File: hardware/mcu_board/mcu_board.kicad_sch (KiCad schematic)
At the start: 1 part, among them J7 MCU

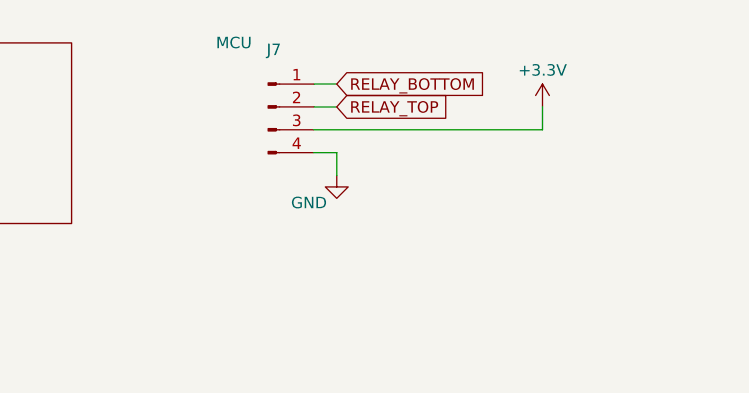
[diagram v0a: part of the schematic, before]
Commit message: Refactored PCBs for v2. See README
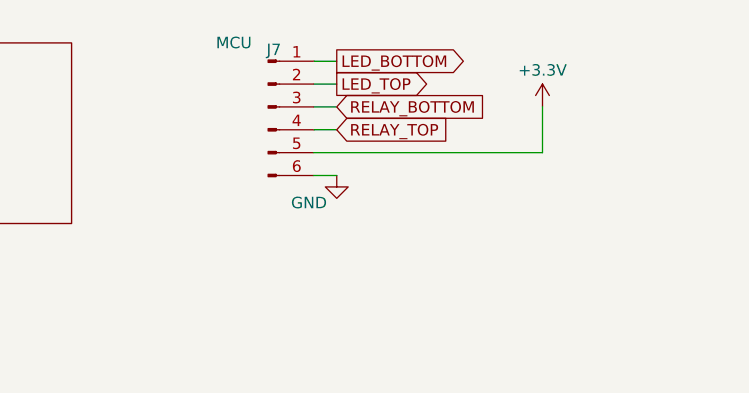
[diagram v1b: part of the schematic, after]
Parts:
- J7: footprint Connector_PinHeader_2.54mm:PinHeader_1x04_P2.54mm_Horizontal -> Connector_PinHeader_2.54mm:PinHeader_1x06_P2.54mm_Horizontal; symbol Connector:Conn_01x04_Pin -> Connector:Conn_01x06_Pin
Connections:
- net +3.3V: now also J7.5 (Pin_5); no longer J7.3 (Pin_3)
- net GND: now also J7.6 (Pin_6); no longer J7.4 (Pin_4)
- net RELAY_BOTTOM: now also J7.3 (Pin_3); no longer J7.1 (Pin_1)
- net RELAY_TOP: now also J7.4 (Pin_4); no longer J7.2 (Pin_2)
- new net LED_BOTTOM: J7.1 (Pin_1)
- new net LED_TOP: J7.2 (Pin_2)
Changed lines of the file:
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@@
 (kicad_sch (version 20230121) (generator eeschema)
   (paper "A4")
-  (wire (pts (xy 144.78 35.56) (xy 147.32 35.56))
-    (stroke (width 0) (type default))
-  )
-  (wire (pts (xy 144.78 43.18) (xy 147.32 43.18))
-    (stroke (width 0) (type default))
-  )
   (wire (pts (xy 144.78 38.1) (xy 147.32 38.1))
     (stroke (width 0) (type default))
   )
-  (wire (pts (xy 144.78 40.64) (xy 170.18 40.64))
+  (wire (pts (xy 144.78 43.18) (xy 170.18 43.18))
     (stroke (width 0) (type default))
   )
-  (wire (pts (xy 170.18 38.1) (xy 170.18 40.64))
+  (wire (pts (xy 144.78 45.72) (xy 147.32 45.72))
     (stroke (width 0) (type default))
   )
-  (wire (pts (xy 147.32 43.18) (xy 147.32 45.72))
+  (wire (pts (xy 144.78 40.64) (xy 147.32 40.64))
+    (stroke (width 0) (type default))
+  )
+  (wire (pts (xy 170.18 38.1) (xy 170.18 43.18))
+    (stroke (width 0) (type default))
+  )
+  (wire (pts (xy 144.78 33.02) (xy 147.32 33.02))
+    (stroke (width 0) (type default))
+  )
+  (wire (pts (xy 144.78 35.56) (xy 147.32 35.56))
     (stroke (width 0) (type default))
   )
@@
     (effects (font (size 1.27 1.27)) (justify left top))
   )
-  (global_label "RELAY_TOP" (shape input) (at 147.32 38.1 0) (fields_autoplaced)
+  (global_label "RELAY_TOP" (shape input) (at 147.32 40.64 0) (fields_autoplaced)
     (effects (font (size 1.27 1.27)) (justify left))
-    (property "Intersheetrefs" "${INTERSHEET_REFS}" (at 160.3858 38.1 0)
+    (property "Intersheetrefs" "${INTERSHEET_REFS}" (at 160.3858 40.64 0)
       (effects (font (size 1.27 1.27)) (justify left) hide)
     )
   )
-  (global_label "RELAY_BOTTOM" (shape input) (at 147.32 35.56 0) (fields_autoplaced)
+  (global_label "LED_TOP" (shape output) (at 147.32 35.56 0) (fields_autoplaced)
     (effects (font (size 1.27 1.27)) (justify left))
-    (property "Intersheetrefs" "${INTERSHEET_REFS}" (at 164.1353 35.56 0)
+    (property "Intersheetrefs" "${INTERSHEET_REFS}" (at 158.288 35.56 0)
+      (effects (font (size 1.27 1.27)) (justify left) hide)
+    )
+  )
+  (global_label "LED_BOTTOM" (shape output) (at 147.32 33.02 0) (fields_autoplaced)
+    (effects (font (size 1.27 1.27)) (justify left))
+    (property "Intersheetrefs" "${INTERSHEET_REFS}" (at 162.0375 33.02 0)
+      (effects (font (size 1.27 1.27)) (justify left) hide)
+    )
+  )
+  (global_label "RELAY_BOTTOM" (shape input) (at 147.32 38.1 0) (fields_autoplaced)
+    (effects (font (size 1.27 1.27)) (justify left))
+    (property "Intersheetrefs" "${INTERSHEET_REFS}" (at 164.1353 38.1 0)
       (effects (font (size 1.27 1.27)) (justify left) hide)
     )
@@
     (pin "1")
     (instances
-      (project "immersion-controller"
+      (project "mcu_board"
         (path "/bd6e6743-d7bb-4018-a688-d589a8d21d49"
           (reference "#PWR01") (unit 1)
@@
     )
   )
-  (symbol (lib_id "Connector:Conn_01x04_Pin") (at 139.7 38.1 0) (unit 1)
+  (symbol (lib_id "Connector:Conn_01x06_Pin") (at 139.7 38.1 0) (unit 1)
     (in_bom yes) (on_board yes) (dnp no)
     (property "Reference" "J7" (at 140.335 31.75 0)
@@
       (effects (font (size 1.27 1.27)))
     )
-    (property "Footprint" "Connector_PinHeader_2.54mm:PinHeader_1x04_P2.54mm_Horizontal" (at 139.7 38.1 0)
+    (property "Footprint" "Connector_PinHeader_2.54mm:PinHeader_1x06_P2.54mm_Horizontal" (at 139.7 38.1 0)
       (effects (font (size 1.27 1.27)) hide)
     )
@@
     (pin "3")
     (pin "4")
+    (pin "5")
+    (pin "6")
     (instances
-      (project "immersion-controller"
+      (project "mcu_board"
         (path "/bd6e6743-d7bb-4018-a688-d589a8d21d49"
           (reference "J7") (unit 1)
@@
     (pin "1")
     (instances
-      (project "immersion-controller"
+      (project "mcu_board"
         (path "/bd6e6743-d7bb-4018-a688-d589a8d21d49"
           (reference "#PWR02") (unit 1)
@@
     )
     (instances
-      (project "immersion-controller"
+      (project "mcu_board"
         (path "/bd6e6743-d7bb-4018-a688-d589a8d21d49" (page "4"))
       )

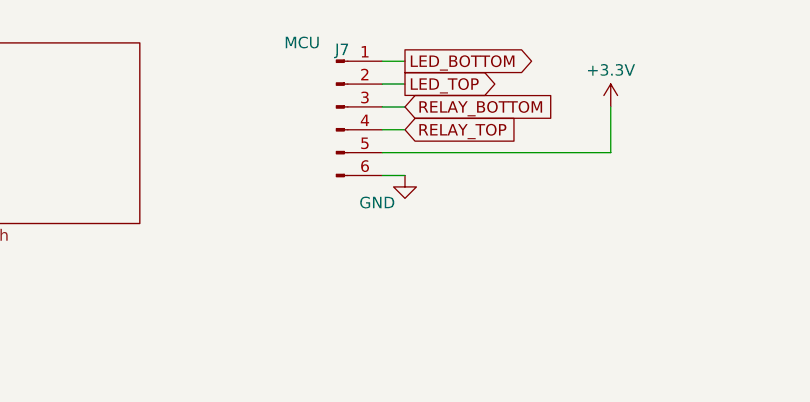
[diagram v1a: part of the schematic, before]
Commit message: v2 layout changes to fit in bax
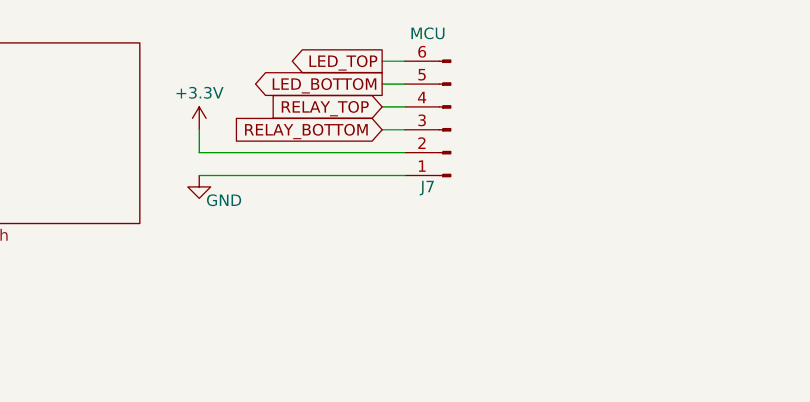
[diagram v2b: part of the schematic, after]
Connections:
- net +3.3V: now also J7.2 (Pin_2); no longer J7.5 (Pin_5)
- net GND: now also J7.1 (Pin_1); no longer J7.6 (Pin_6)
- net LED_BOTTOM: now also J7.5 (Pin_5); no longer J7.1 (Pin_1)
- net LED_TOP: now also J7.6 (Pin_6); no longer J7.2 (Pin_2)
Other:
- moved on the sheet: J7
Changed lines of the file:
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@@
 (kicad_sch (version 20230121) (generator eeschema)
   (paper "A4")
-  (wire (pts (xy 144.78 38.1) (xy 147.32 38.1))
-    (stroke (width 0) (type default))
-  )
-  (wire (pts (xy 144.78 43.18) (xy 170.18 43.18))
-    (stroke (width 0) (type default))
-  )
-  (wire (pts (xy 144.78 45.72) (xy 147.32 45.72))
+  (wire (pts (xy 144.78 33.02) (xy 147.32 33.02))
     (stroke (width 0) (type default))
   )
@@
     (stroke (width 0) (type default))
   )
-  (wire (pts (xy 170.18 38.1) (xy 170.18 43.18))
+  (wire (pts (xy 144.78 35.56) (xy 147.32 35.56))
     (stroke (width 0) (type default))
   )
-  (wire (pts (xy 144.78 33.02) (xy 147.32 33.02))
+  (wire (pts (xy 144.78 38.1) (xy 147.32 38.1))
     (stroke (width 0) (type default))
   )
-  (wire (pts (xy 144.78 35.56) (xy 147.32 35.56))
+  (wire (pts (xy 124.46 45.72) (xy 147.32 45.72))
+    (stroke (width 0) (type default))
+  )
+  (wire (pts (xy 124.46 43.18) (xy 147.32 43.18))
+    (stroke (width 0) (type default))
+  )
+  (wire (pts (xy 124.46 40.64) (xy 124.46 43.18))
     (stroke (width 0) (type default))
   )
@@
     (effects (font (size 1.27 1.27)) (justify left top))
   )
-  (global_label "RELAY_TOP" (shape input) (at 147.32 40.64 0) (fields_autoplaced)
-    (effects (font (size 1.27 1.27)) (justify left))
-    (property "Intersheetrefs" "${INTERSHEET_REFS}" (at 160.3858 40.64 0)
-      (effects (font (size 1.27 1.27)) (justify left) hide)
+  (global_label "RELAY_TOP" (shape input) (at 144.78 38.1 180) (fields_autoplaced)
+    (effects (font (size 1.27 1.27)) (justify right))
+    (property "Intersheetrefs" "${INTERSHEET_REFS}" (at 131.6348 38.1 0)
+      (effects (font (size 1.27 1.27)) (justify right) hide)
     )
   )
-  (global_label "LED_TOP" (shape output) (at 147.32 35.56 0) (fields_autoplaced)
-    (effects (font (size 1.27 1.27)) (justify left))
-    (property "Intersheetrefs" "${INTERSHEET_REFS}" (at 158.288 35.56 0)
-      (effects (font (size 1.27 1.27)) (justify left) hide)
+  (global_label "LED_TOP" (shape output) (at 144.78 33.02 180) (fields_autoplaced)
+    (effects (font (size 1.27 1.27)) (justify right))
+    (property "Intersheetrefs" "${INTERSHEET_REFS}" (at 133.812 33.02 0)
+      (effects (font (size 1.27 1.27)) (justify right) hide)
     )
   )
-  (global_label "LED_BOTTOM" (shape output) (at 147.32 33.02 0) (fields_autoplaced)
-    (effects (font (size 1.27 1.27)) (justify left))
-    (property "Intersheetrefs" "${INTERSHEET_REFS}" (at 162.0375 33.02 0)
-      (effects (font (size 1.27 1.27)) (justify left) hide)
+  (global_label "LED_BOTTOM" (shape output) (at 144.78 35.56 180) (fields_autoplaced)
+    (effects (font (size 1.27 1.27)) (justify right))
+    (property "Intersheetrefs" "${INTERSHEET_REFS}" (at 130.0625 35.56 0)
+      (effects (font (size 1.27 1.27)) (justify right) hide)
     )
   )
-  (global_label "RELAY_BOTTOM" (shape input) (at 147.32 38.1 0) (fields_autoplaced)
-    (effects (font (size 1.27 1.27)) (justify left))
-    (property "Intersheetrefs" "${INTERSHEET_REFS}" (at 164.1353 38.1 0)
-      (effects (font (size 1.27 1.27)) (justify left) hide)
+  (global_label "RELAY_BOTTOM" (shape input) (at 144.78 40.64 180) (fields_autoplaced)
+    (effects (font (size 1.27 1.27)) (justify right))
+    (property "Intersheetrefs" "${INTERSHEET_REFS}" (at 127.8853 40.64 0)
+      (effects (font (size 1.27 1.27)) (justify right) hide)
     )
   )
-  (symbol (lib_id "power:+3.3V") (at 170.18 38.1 0) (unit 1)
+  (symbol (lib_id "power:+3.3V") (at 124.46 40.64 0) (unit 1)
     (in_bom yes) (on_board yes) (dnp no) (fields_autoplaced)
-    (property "Reference" "#PWR01" (at 170.18 41.91 0)
+    (property "Reference" "#PWR01" (at 124.46 44.45 0)
       (effects (font (size 1.27 1.27)) hide)
     )
-    (property "Value" "+3.3V" (at 170.18 34.036 0)
+    (property "Value" "+3.3V" (at 124.46 36.576 0)
       (effects (font (size 1.27 1.27)))
     )
-    (property "Footprint" "" (at 170.18 38.1 0)
+    (property "Footprint" "" (at 124.46 40.64 0)
       (effects (font (size 1.27 1.27)) hide)
     )
-    (property "Datasheet" "" (at 170.18 38.1 0)
+    (property "Datasheet" "" (at 124.46 40.64 0)
       (effects (font (size 1.27 1.27)) hide)
     )
@@
     )
   )
-  (symbol (lib_id "Connector:Conn_01x06_Pin") (at 139.7 38.1 0) (unit 1)
+  (symbol (lib_id "Connector:Conn_01x06_Pin") (at 152.4 40.64 180) (unit 1)
     (in_bom yes) (on_board yes) (dnp no)
-    (property "Reference" "J7" (at 140.335 31.75 0)
+    (property "Reference" "J7" (at 149.86 46.99 0)
       (effects (font (size 1.27 1.27)))
     )
-    (property "Value" "MCU" (at 135.89 30.988 0)
+    (property "Value" "MCU" (at 149.86 29.972 0)
       (effects (font (size 1.27 1.27)))
     )
-    (property "Footprint" "Connector_PinHeader_2.54mm:PinHeader_1x06_P2.54mm_Horizontal" (at 139.7 38.1 0)
+    (property "Footprint" "Connector_PinHeader_2.54mm:PinHeader_1x06_P2.54mm_Horizontal" (at 152.4 40.64 0)
       (effects (font (size 1.27 1.27)) hide)
     )
-    (property "Datasheet" "~" (at 139.7 38.1 0)
+    (property "Datasheet" "~" (at 152.4 40.64 0)
       (effects (font (size 1.27 1.27)) hide)
     )
@@
     )
   )
-  (symbol (lib_id "power:GND") (at 147.32 45.72 0) (unit 1)
+  (symbol (lib_id "power:GND") (at 124.46 45.72 0) (unit 1)
     (in_bom yes) (on_board yes) (dnp no)
-    (property "Reference" "#PWR02" (at 147.32 52.07 0)
+    (property "Reference" "#PWR02" (at 124.46 52.07 0)
       (effects (font (size 1.27 1.27)) hide)
     )
-    (property "Value" "GND" (at 142.24 48.768 0)
+    (property "Value" "GND" (at 125.222 48.514 0)
       (effects (font (size 1.27 1.27)) (justify left))
     )
-    (property "Footprint" "" (at 147.32 45.72 0)
+    (property "Footprint" "" (at 124.46 45.72 0)
       (effects (font (size 1.27 1.27)) hide)
     )
-    (property "Datasheet" "" (at 147.32 45.72 0)
+    (property "Datasheet" "" (at 124.46 45.72 0)
       (effects (font (size 1.27 1.27)) hide)
     )

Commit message: Laypout tweaks to fit case
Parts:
- added J2: LEDS_OUT, Connector_PinHeader_2.54mm:PinHeader_1x03_P2.54mm_Vertical, symbol Connector_Generic:Conn_01x03
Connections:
- net +3.3V: now also J2.3 (Pin_3)
- net LED_BOTTOM: now also J2.1 (Pin_1)
- net LED_TOP: now also J2.2 (Pin_2)
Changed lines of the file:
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@@
 (kicad_sch (version 20230121) (generator eeschema)
   (paper "A4")
+  (junction (at 147.32 33.02) (diameter 0) (color 0 0 0 0)
+  )
+  (junction (at 147.32 35.56) (diameter 0) (color 0 0 0 0)
+  )
+  (junction (at 147.32 43.18) (diameter 0) (color 0 0 0 0)
+  )
   (wire (pts (xy 144.78 33.02) (xy 147.32 33.02))
     (stroke (width 0) (type default))
   )
   (wire (pts (xy 144.78 40.64) (xy 147.32 40.64))
+    (stroke (width 0) (type default))
+  )
+  (wire (pts (xy 172.72 43.18) (xy 147.32 43.18))
+    (stroke (width 0) (type default))
+  )
+  (wire (pts (xy 168.91 35.56) (xy 172.72 35.56))
+    (stroke (width 0) (type default))
+  )
+  (wire (pts (xy 147.32 27.94) (xy 168.91 27.94))
     (stroke (width 0) (type default))
   )
@@
     (stroke (width 0) (type default))
   )
+  (wire (pts (xy 161.29 35.56) (xy 147.32 35.56))
+    (stroke (width 0) (type default))
+  )
+  (wire (pts (xy 147.32 27.94) (xy 147.32 33.02))
+    (stroke (width 0) (type default))
+  )
+  (wire (pts (xy 161.29 33.02) (xy 161.29 35.56))
+    (stroke (width 0) (type default))
+  )
+  (wire (pts (xy 172.72 33.02) (xy 161.29 33.02))
+    (stroke (width 0) (type default))
+  )
   (wire (pts (xy 124.46 45.72) (xy 147.32 45.72))
+    (stroke (width 0) (type default))
+  )
+  (wire (pts (xy 168.91 27.94) (xy 168.91 35.56))
     (stroke (width 0) (type default))
   )
@@
   )
   (wire (pts (xy 124.46 40.64) (xy 124.46 43.18))
+    (stroke (width 0) (type default))
+  )
+  (wire (pts (xy 172.72 38.1) (xy 172.72 43.18))
     (stroke (width 0) (type default))
   )
@@
         )
       )
+    )
+  )
+  (symbol (lib_id "Connector_Generic:Conn_01x03") (at 177.8 35.56 0) (unit 1)
+    (in_bom yes) (on_board yes) (dnp no) (fields_autoplaced)
+    (property "Reference" "J2" (at 180.34 34.29 0)
+      (effects (font (size 1.27 1.27)) (justify left))
+    )
+    (property "Value" "LEDS_OUT" (at 180.34 36.83 0)
+      (effects (font (size 1.27 1.27)) (justify left))
+    )
+    (property "Footprint" "Connector_PinHeader_2.54mm:PinHeader_1x03_P2.54mm_Vertical" (at 177.8 35.56 0)
+      (effects (font (size 1.27 1.27)) hide)
+    )
+    (property "Datasheet" "~" (at 177.8 35.56 0)
+      (effects (font (size 1.27 1.27)) hide)
+    )
+    (pin "1")
+    (pin "2")
+    (pin "3")
+    (instances
+      (project "mcu_board"
+        (path "/bd6e6743-d7bb-4018-a688-d589a8d21d49"
+          (reference "J2") (unit 1)
+        )
+        (path "/bd6e6743-d7bb-4018-a688-d589a8d21d49/c342793f-dc31-48ad-871b-028ebc2ab27d"
+          (reference "J2") (unit 1)
+        )
+      )

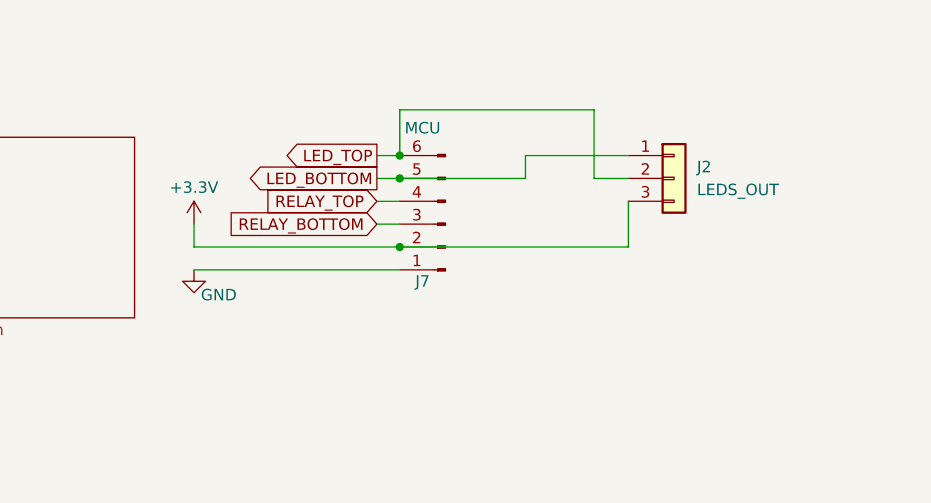
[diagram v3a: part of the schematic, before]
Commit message: fix boards so they components are on the correct side lol
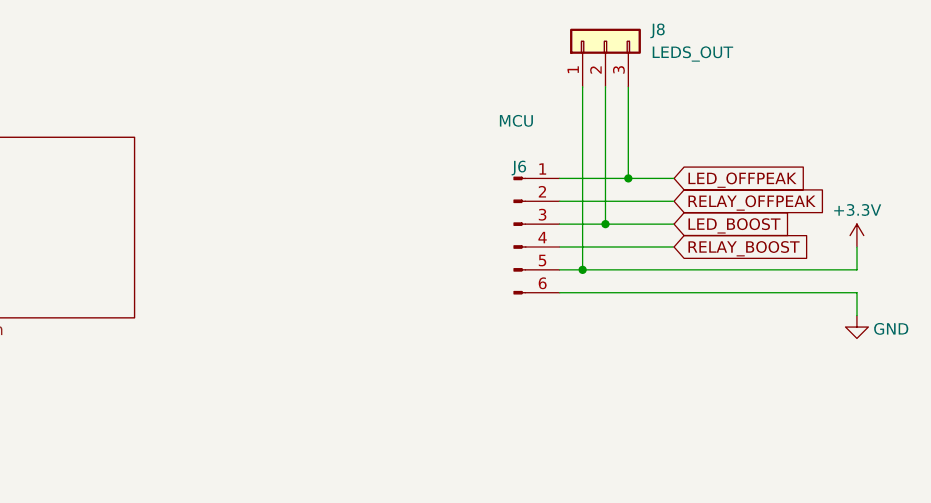
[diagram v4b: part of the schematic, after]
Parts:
- removed J2: LEDS_OUT, Connector_PinHeader_2.54mm:PinHeader_1x03_P2.54mm_Vertical, symbol Connector_Generic:Conn_01x03
- removed J7: MCU, Connector_PinHeader_2.54mm:PinHeader_1x06_P2.54mm_Horizontal, symbol Connector:Conn_01x06_Pin
- added J6: MCU, Connector_PinHeader_2.54mm:PinHeader_1x06_P2.54mm_Vertical, symbol Connector:Conn_01x06_Pin
- added J8: LEDS_OUT, Connector_PinHeader_2.54mm:PinHeader_1x03_P2.54mm_Vertical, symbol Connector_Generic:Conn_01x03
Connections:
- net +3.3V: now also J6.5 (Pin_5), J8.1 (Pin_1)
- net GND: now also J6.6 (Pin_6)
- new net LED_BOOST: J6.3 (Pin_3), J8.2 (Pin_2)
- new net LED_OFFPEAK: J6.1 (Pin_1), J8.3 (Pin_3)
- new net RELAY_BOOST: J6.4 (Pin_4)
- new net RELAY_OFFPEAK: J6.2 (Pin_2)
